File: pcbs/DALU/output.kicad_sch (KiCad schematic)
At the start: 6 parts, among them U801 74HC74, U802 74HC32, U803 74HCT574

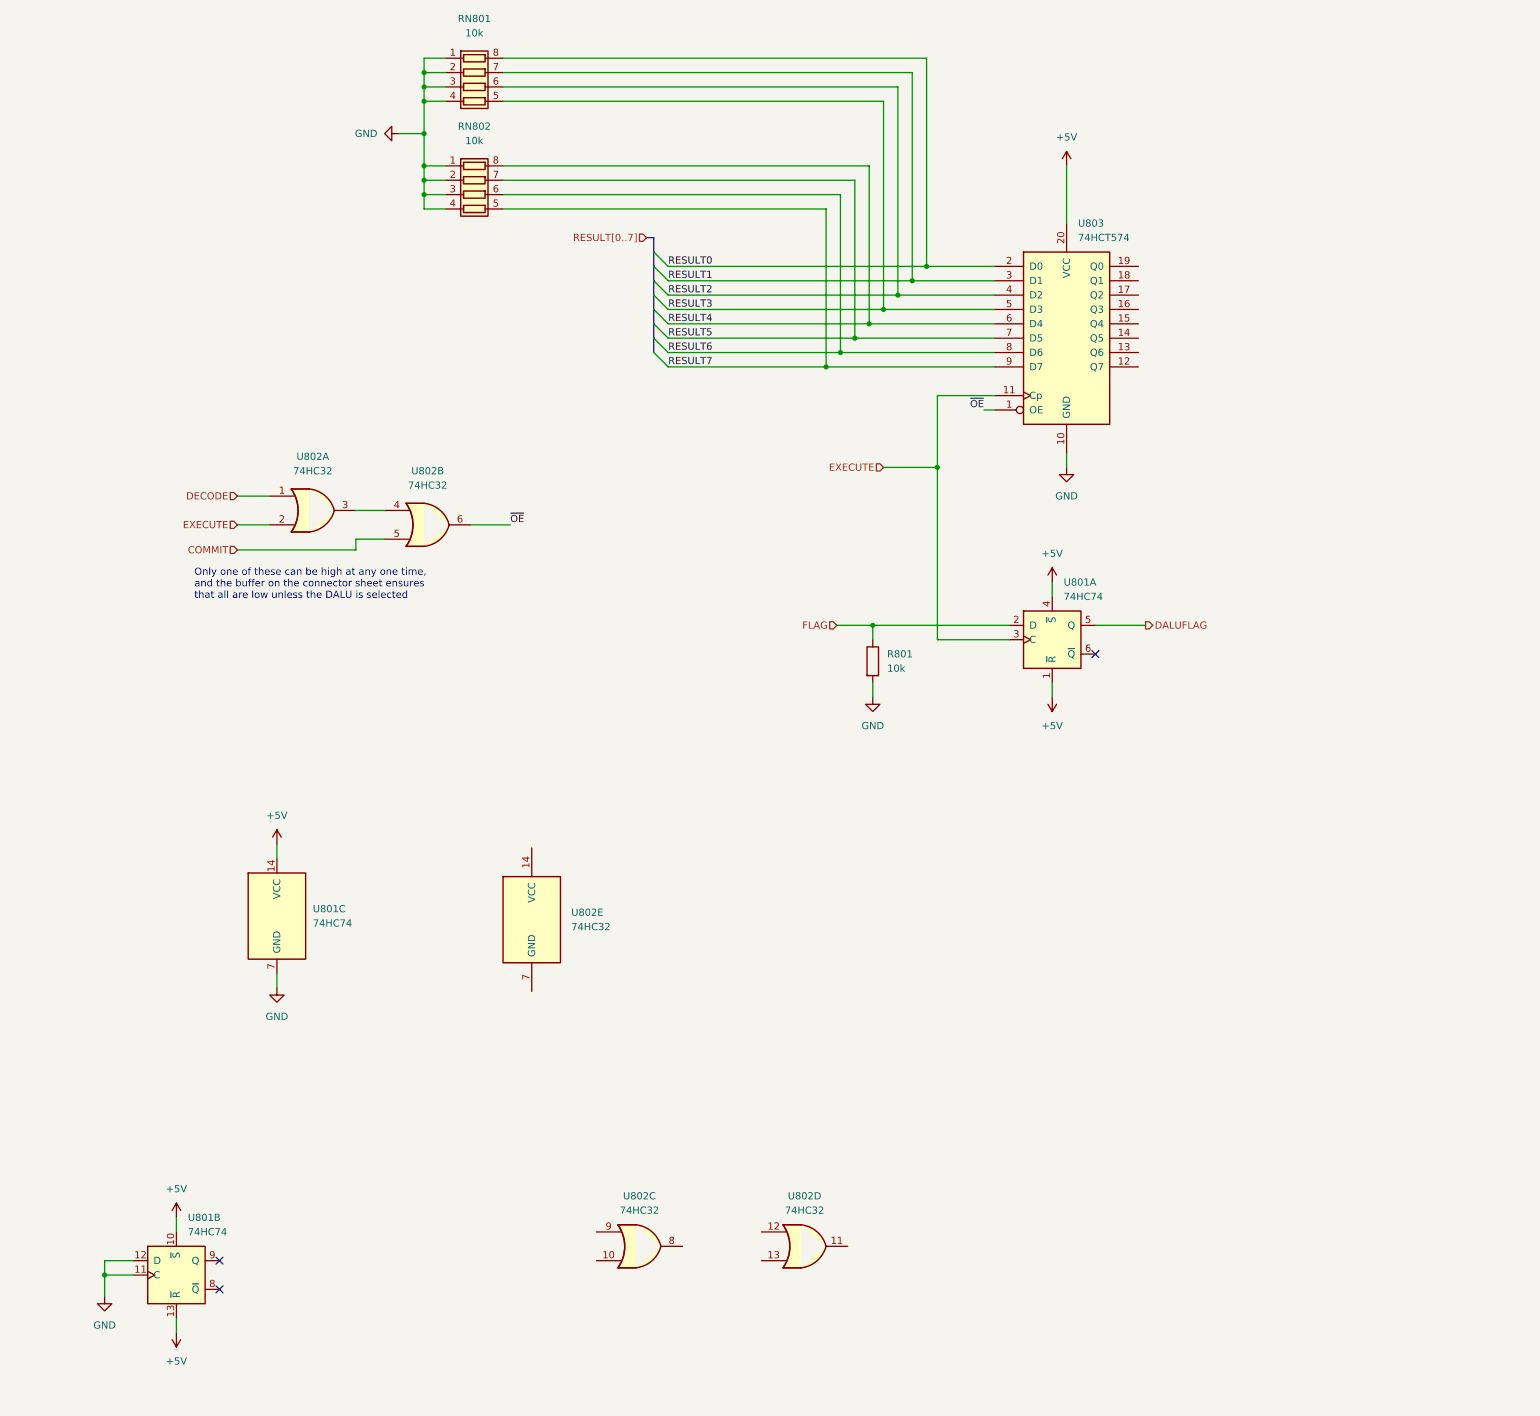
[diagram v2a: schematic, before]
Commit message: Redoing resistors
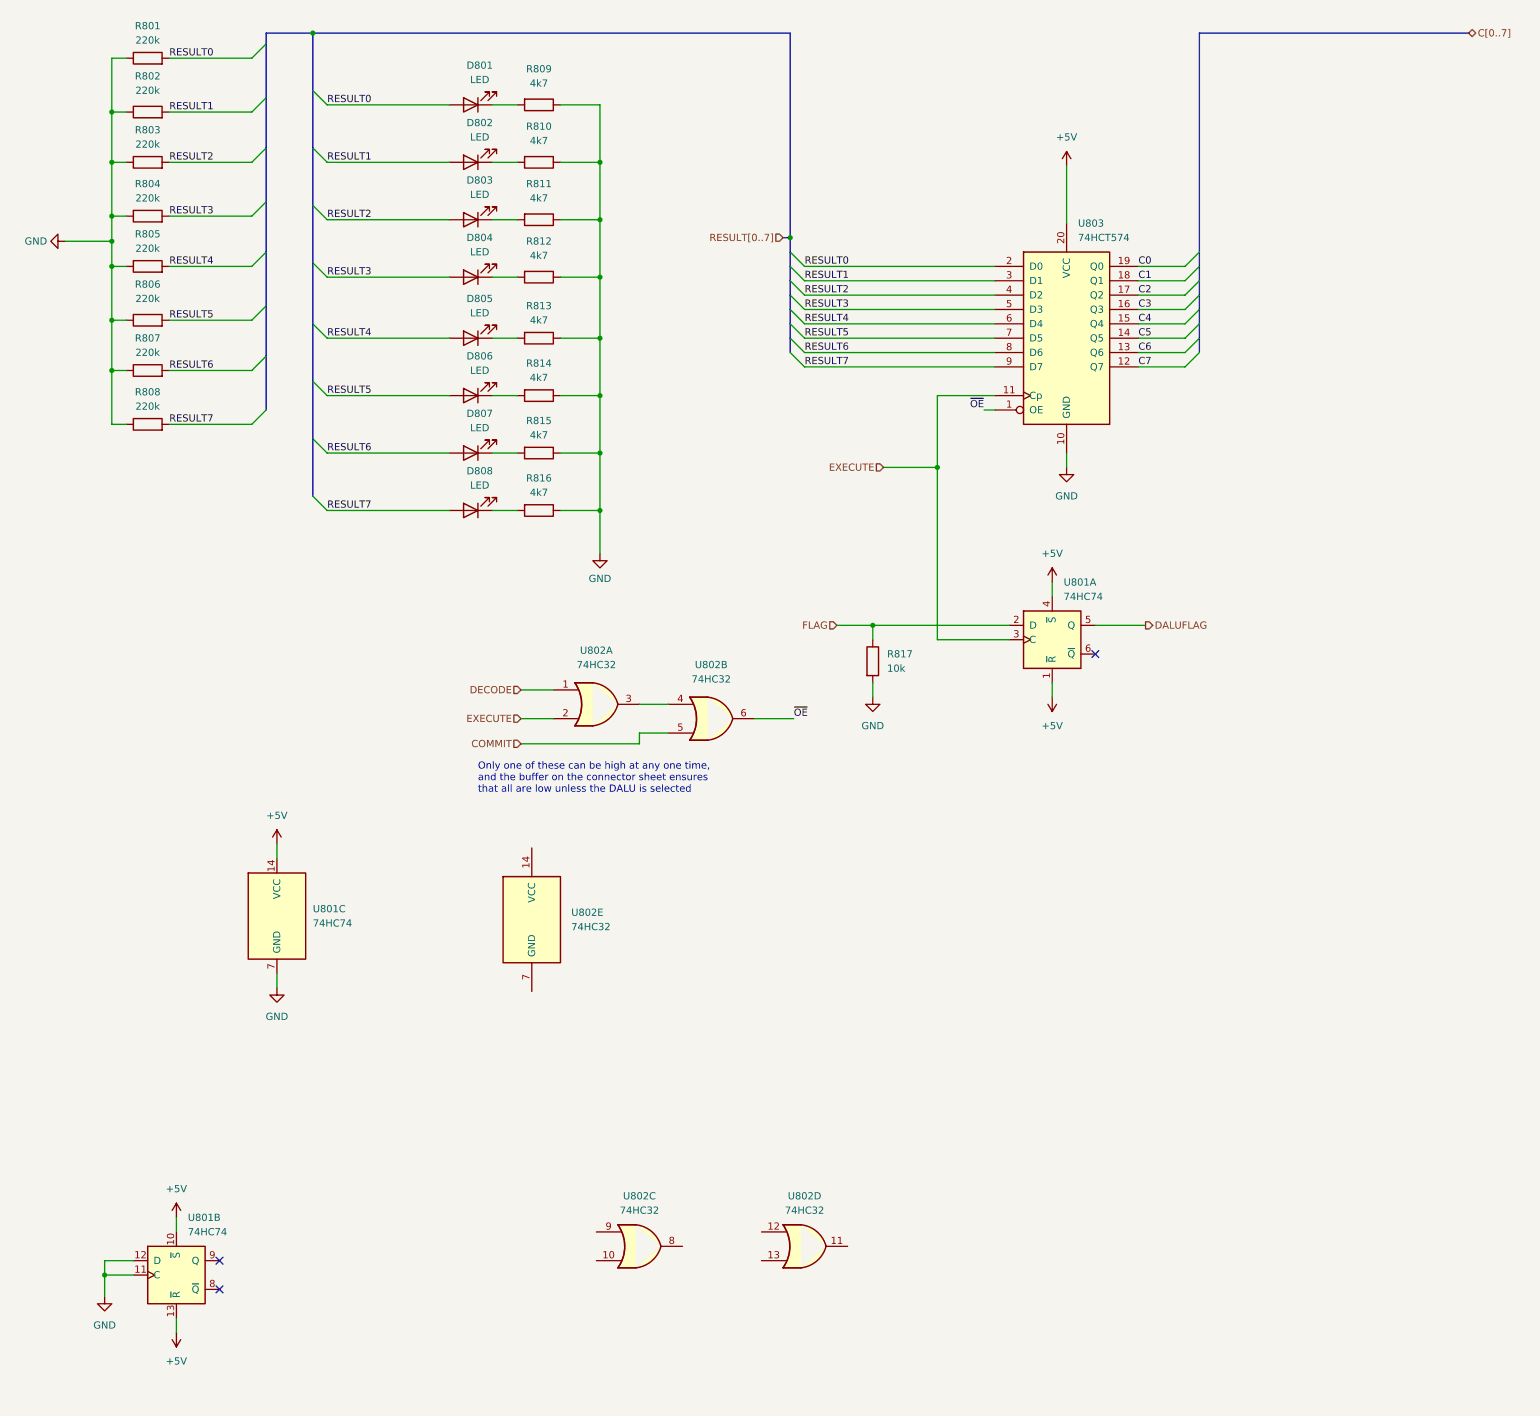
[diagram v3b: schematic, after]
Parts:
- removed RN801, RN802: 10k, Resistor_SMD:R_Array_Convex_4x0402, symbol Device:R_Pack04
- added D801, D802, D803, D804, D805, D806, D807, D808: LED, LED_SMD:LED_0603_1608Metric, symbol Device:LED
- added R801, R802, R803, R804, R805, R806, R807, R808: 220k, Resistor_SMD:R_0603_1608Metric, symbol Device:R
- added R809, R810, R811, R812, R813, R814, R815, R816: 4k7, Resistor_SMD:R_0603_1608Metric, symbol Device:R
- renumbered R801 to R817
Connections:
- net GND: now also R801.1, R802.1, R803.1, R804.1, R805.1, R806.1, R807.1, R808.1, R809.1, R810.1, R811.1, R812.1, R813.1, R814.1, R815.1, R816.1
- net RESULT0: now also D801.2 (A), R801.2
- net RESULT1: now also D802.2 (A), R802.2
- net RESULT2: now also D803.2 (A), R803.2
- net RESULT3: now also D804.2 (A), R804.2
- net RESULT4: now also D805.2 (A), R805.2
- net RESULT5: now also D806.2 (A), R806.2
- net RESULT6: now also D807.2 (A), R807.2
- net RESULT7: now also D808.2 (A), R808.2
- net C7: now reaches U803.12 (Q7)
- net C6: now reaches U803.13 (Q6)
- net C5: now reaches U803.14 (Q5)
- net C4: now reaches U803.15 (Q4)
- net C3: now reaches U803.16 (Q3)
- net C2: now reaches U803.17 (Q2)
- net C1: now reaches U803.18 (Q1)
- net C0: now reaches U803.19 (Q0)
- new net: D801.1 (K), R809.2
- new net: D802.1 (K), R810.2
- new net: D803.1 (K), R811.2
- new net: D805.1 (K), R813.2
- new net: D807.1 (K), R815.2
- new net: D804.1 (K), R812.2
- new net: D806.1 (K), R814.2
- new net: D808.1 (K), R816.2
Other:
- moved on the sheet: U802A, U802B

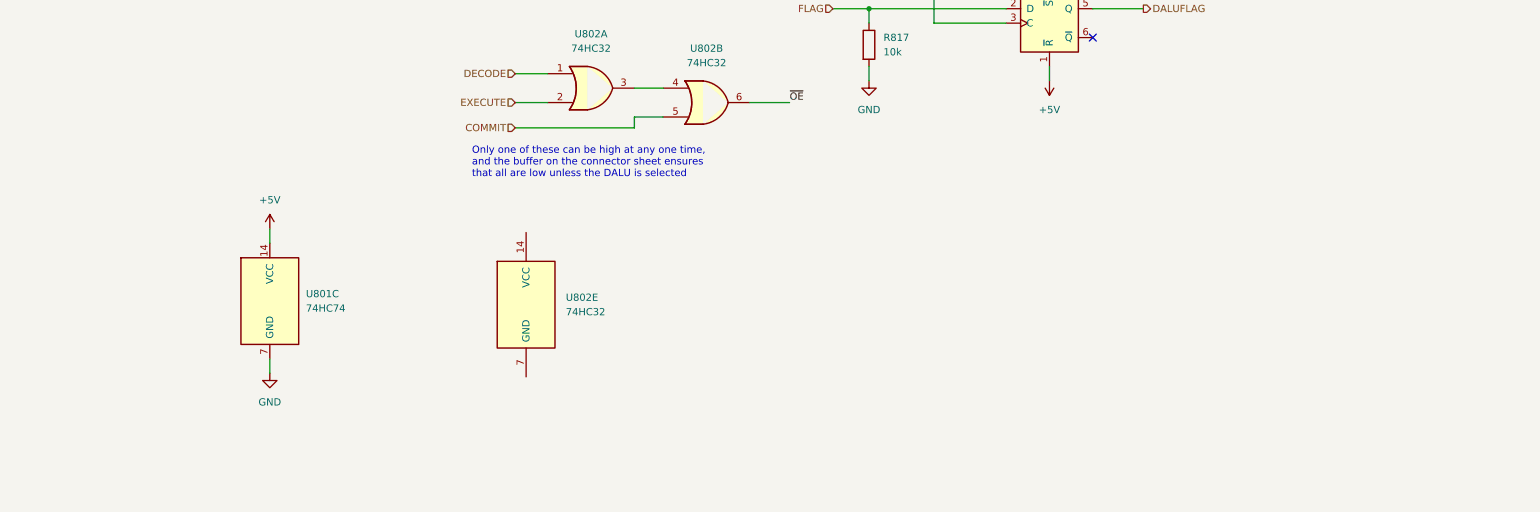
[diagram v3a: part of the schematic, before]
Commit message: Starting to connect up control wires
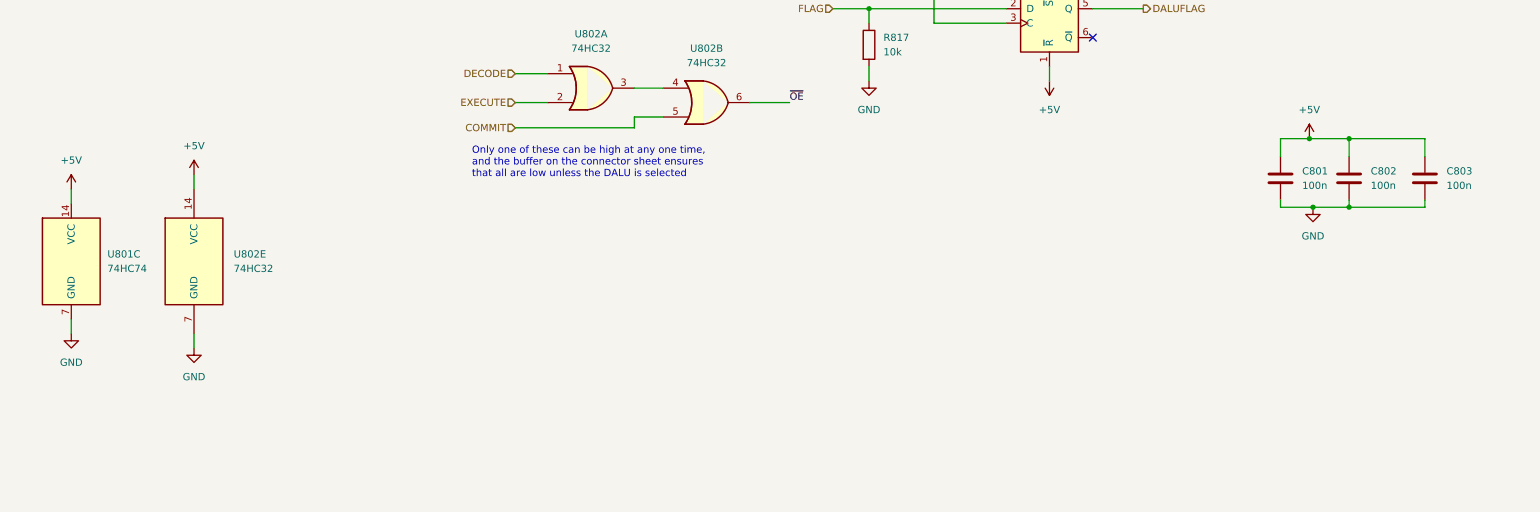
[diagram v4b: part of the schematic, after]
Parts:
- added C801, C802, C803: 100n, Capacitor_SMD:C_0603_1608Metric, symbol Device:C
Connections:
- net +5V: now also U802.14 (VCC), C801.1, C802.1, C803.1
- net GND: now also U802.7 (GND), C801.2, C802.2, C803.2
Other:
- moved on the sheet: U801C, U802E
